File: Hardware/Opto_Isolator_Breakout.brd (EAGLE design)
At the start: 15.2 x 12.7 mm, 16 parts, among them Q1 NPN, Q2 NPN, U1 OPTO

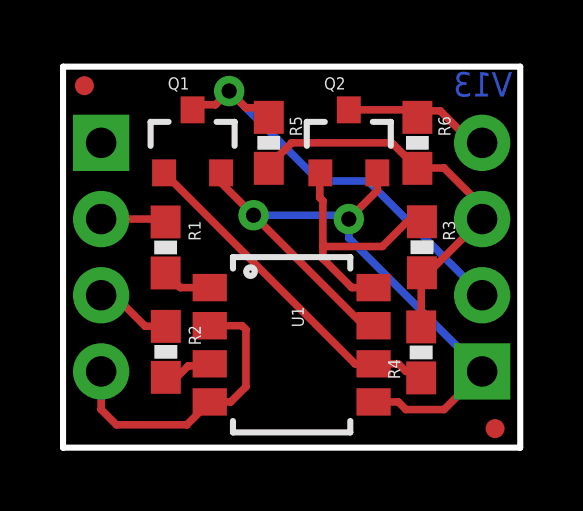
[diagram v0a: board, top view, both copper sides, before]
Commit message: Added attributes for IC IDL213T
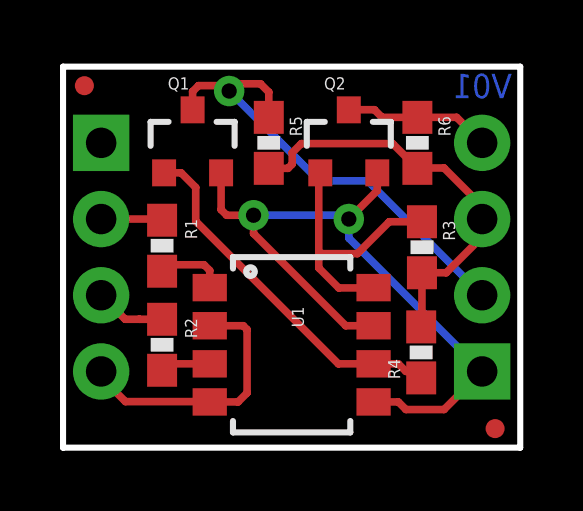
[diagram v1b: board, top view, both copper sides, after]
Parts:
- Q1, Q2: device SparkFun:SOT23-3 -> SparkFun-DiscreteSemi:SOT23-3
- R1, R2: value 200k -> 220
- U1: value OPTO -> OPTOISOLATOR-2SOIC8; device SparkFun:SO08-2 -> SparkFun-DiscreteSemi:SO08-2
- moved FRAME1 9.16 mm to (-22.7, -12.7)
- moved R2 0.27 mm to (3.30, 3.43)
- moved R1 0.13 mm to (3.30, 6.73)
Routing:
- net GND: track 10.00 -> 8.93 mm
- net OUT2: track 14.9 -> 15.9 mm
- net HV-GND: track 23.7 -> 24.6 mm
- net OUT2N: track 11.4 -> 12.1 mm
- net N$1: track 1.67 -> 2.33 mm
- net OUT1N: track 8.65 -> 9.25 mm
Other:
- board text added: "V01"
- board text removed: "V13"

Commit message: Fixed qc checklist issues.
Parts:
- FRAME1: value FRAME-LETTER -> (none)
- moved LOGO1 0.32 mm to (7.62, 8.45)
- moved LOGO2 0.16 mm to (8.71, 3.75)
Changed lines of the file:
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@@
 <setting verticaltext="up"/>
 </settings>
-<grid distance="0.05" unitdist="inch" unit="inch" style="lines" multiple="1" display="yes" altdistance="0.005" altunitdist="inch" altunit="inch"/>
+<grid distance="0.05" unitdist="inch" unit="inch" style="lines" multiple="1" display="yes" altdistance="0.00001" altunitdist="inch" altunit="inch"/>
 <layers>
 <layer number="1" name="Top" color="4" fill="1" visible="yes" active="yes"/>
@@
 <layer number="56" name="wert" color="7" fill="1" visible="no" active="yes"/>
 <layer number="57" name="tCAD" color="7" fill="1" visible="no" active="no"/>
+<layer number="59" name="tCarbon" color="7" fill="1" visible="no" active="no"/>
+<layer number="60" name="bCarbon" color="7" fill="1" visible="no" active="no"/>
 <layer number="90" name="Modules" color="5" fill="1" visible="no" active="no"/>
 <layer number="91" name="Nets" color="2" fill="1" visible="no" active="no"/>
@@
 <layer number="127" name="_tValues" color="7" fill="1" visible="no" active="yes"/>
 <layer number="128" name="_bValues" color="7" fill="1" visible="no" active="yes"/>
+<layer number="129" name="Mask" color="7" fill="1" visible="yes" active="yes"/>
 <layer number="131" name="tAdjust" color="7" fill="1" visible="no" active="yes"/>
 <layer number="132" name="bAdjust" color="7" fill="1" visible="no" active="yes"/>
@@
 <layer number="251" name="SMDround" color="12" fill="11" visible="no" active="no"/>
 <layer number="254" name="cooling" color="7" fill="1" visible="no" active="yes"/>
+<layer number="255" name="routoute" color="7" fill="1" visible="yes" active="yes"/>
 </layers>
 <board>
@@
 <element name="U$2" library="SparkFun-Aesthetics" package="MICRO-FIDUCIAL" value="FIDUCIALUFIDUCIAL" x="0.7112" y="12.065"/>
 <element name="U$3" library="SparkFun-Aesthetics" package="MICRO-FIDUCIAL" value="FIDUCIALUFIDUCIAL" x="14.4018" y="0.635"/>
-<element name="FRAME1" library="SparkFun-Aesthetics" package="CREATIVE_COMMONS" value="FRAME-LETTER" x="-22.7215875" y="-12.7"/>
-<element name="LOGO1" library="SparkFun-Aesthetics" package="OSHW-LOGO-S" value="OSHW-LOGOS" x="7.5946" y="8.128" rot="MR0"/>
-<element name="LOGO2" library="SparkFun-Aesthetics" package="SFE_LOGO_FLAME_.1" value="SFE_LOGO_FLAME.1_INCH" x="8.7503" y="3.596640625" rot="MR0"/>
+<element name="FRAME1" library="SparkFun-Aesthetics" package="CREATIVE_COMMONS" value="" x="-22.7215875" y="-12.7">
+<attribute name="VERSION" value="v01" x="-22.7215875" y="-12.7" size="1.778" layer="27" display="off"/>
+<attribute name="DESIGNER" value="NAME" x="-22.7215875" y="-12.7" size="1.778" layer="27" display="off"/>
+</element>
 <element name="R1" library="SparkFun-Resistors" package="0603-RES" value="220" x="3.302" y="6.731" rot="R270">
 <attribute name="PROD_ID" value="RES-07861" x="3.302" y="6.731" size="1.778" layer="27" font="vector" ratio="15" rot="R270" display="off"/>
@@
 <attribute name="PROD_ID" value="RES-07861" x="3.302" y="3.429" size="1.778" layer="27" font="vector" ratio="15" rot="R270" display="off"/>
 </element>
+<element name="LOGO2" library="SparkFun-Aesthetics" package="SFE_LOGO_FLAME_.1" value="SFE_LOGO_FLAME.1_INCH" x="8.710421875" y="3.750309375" rot="MR0"/>
+<element name="LOGO1" library="SparkFun-Aesthetics" package="OSHW-LOGO-S" value="OSHW-LOGOS" x="7.6233" y="8.45134375" rot="MR0"/>
 </elements>
 <signals>

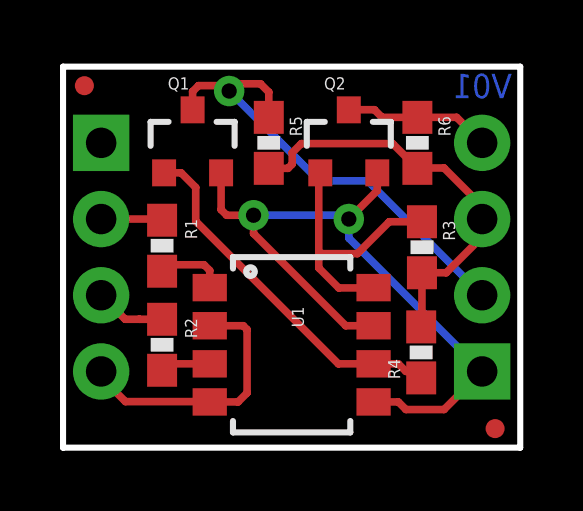
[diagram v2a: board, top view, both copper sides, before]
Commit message: Fixed final qc checklist items.
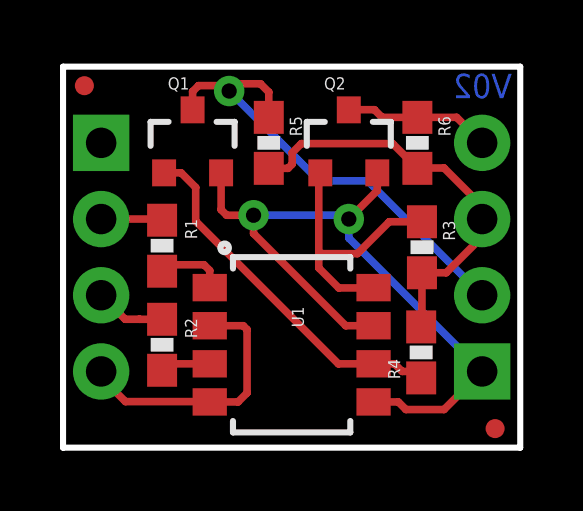
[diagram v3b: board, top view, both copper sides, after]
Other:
- board text added: "V02"
- board text removed: "V01"
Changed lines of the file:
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@@
 <?xml version="1.0" encoding="utf-8"?>
 <!DOCTYPE eagle SYSTEM "eagle.dtd">
-<eagle version="7.1.0">
+<eagle version="6.4">
 <drawing>
 <settings>
@@
 <setting verticaltext="up"/>
 </settings>
-<grid distance="0.05" unitdist="inch" unit="inch" style="lines" multiple="1" display="yes" altdistance="0.00001" altunitdist="inch" altunit="inch"/>
+<grid distance="0.05" unitdist="inch" unit="inch" style="lines" multiple="1" display="yes" altdistance="0.005" altunitdist="inch" altunit="inch"/>
 <layers>
 <layer number="1" name="Top" color="4" fill="1" visible="yes" active="yes"/>
@@
 <layer number="127" name="_tValues" color="7" fill="1" visible="no" active="yes"/>
 <layer number="128" name="_bValues" color="7" fill="1" visible="no" active="yes"/>
-<layer number="129" name="Mask" color="7" fill="1" visible="yes" active="yes"/>
+<layer number="129" name="Mask" color="7" fill="1" visible="no" active="yes"/>
 <layer number="131" name="tAdjust" color="7" fill="1" visible="no" active="yes"/>
 <layer number="132" name="bAdjust" color="7" fill="1" visible="no" active="yes"/>
@@
 <layer number="251" name="SMDround" color="12" fill="11" visible="no" active="no"/>
 <layer number="254" name="cooling" color="7" fill="1" visible="no" active="yes"/>
-<layer number="255" name="routoute" color="7" fill="1" visible="yes" active="yes"/>
+<layer number="255" name="routoute" color="7" fill="1" visible="no" active="yes"/>
 </layers>
 <board>
@@
 <text x="2.794" y="10.668" size="1.016" layer="22" font="vector" ratio="15" rot="MR180">NC</text>
 <text x="12.446" y="0.381" size="1.016" layer="22" font="vector" ratio="15" rot="MR0">Optoisolator</text>
-<text x="14.9606" y="11.6484375" size="0.8128" layer="16" font="vector" ratio="15" rot="MR0">V01</text>
+<text x="14.9606" y="11.6484375" size="0.8128" layer="16" font="vector" ratio="15" rot="MR0">V02</text>
 <text x="-11.140440625" y="-15.60068125" size="1.778" layer="51" font="vector" ratio="10">Revised by: Patrick Alberts</text>
 <text x="7.60221875" y="-12.867640625" size="1.778" layer="51" font="vector" ratio="10">N.Seidle</text>
@@
 <pass name="Default">
 <param name="RoutingGrid" value="50mil"/>
-<param name="AutoGrid" value="1"/>
-<param name="Efforts" value="0"/>
-<param name="TopRouterVariant" value="1"/>
 <param name="tpViaShape" value="round"/>
 <param name="PrefDir.1" value="|"/>
@@
 <contactref element="R4" pad="1"/>
 <contactref element="Q1" pad="1"/>
-<wire x1="10.3505" y1="2.794" x2="11.176" y2="2.794" width="0.254" layer="1"/>
-<wire x1="11.176" y1="2.794" x2="11.43" y2="2.54" width="0.254" layer="1"/>
-<wire x1="11.43" y1="2.54" x2="11.723" y2="2.54" width="0.254" layer="1"/>
+<wire x1="10.3505" y1="2.794" x2="11.049" y2="2.794" width="0.254" layer="1"/>
+<wire x1="11.049" y1="2.794" x2="11.303" y2="2.54" width="0.254" layer="1"/>
+<wire x1="11.303" y1="2.54" x2="11.723" y2="2.54" width="0.254" layer="1"/>
 <wire x1="11.723" y1="2.54" x2="11.938" y2="2.325" width="0.254" layer="1"/>
 <wire x1="3.368" y1="9.16" x2="3.936240625" y2="9.16" width="0.254" layer="1"/>

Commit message: Fixed QC checklist issues
Fixed version # in sch and brd
added "all units in inches" in layer 47
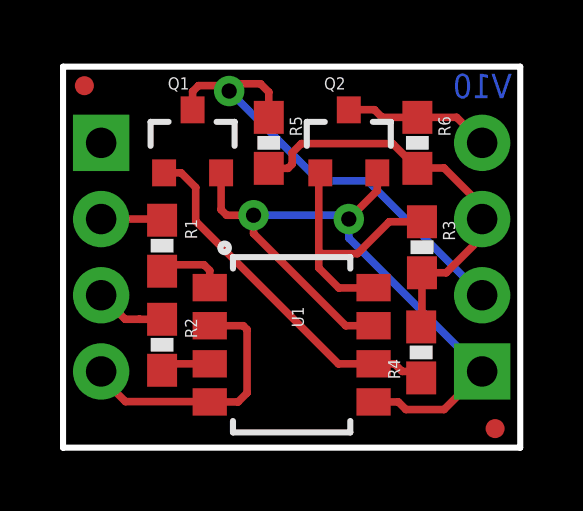
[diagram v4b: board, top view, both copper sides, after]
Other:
- board text added: "All units are in inches."
- board text added: "V10"
- board text removed: "V02"
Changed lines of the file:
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@@
 <?xml version="1.0" encoding="utf-8"?>
 <!DOCTYPE eagle SYSTEM "eagle.dtd">
-<eagle version="6.4">
+<eagle version="7.1.0">
 <drawing>
 <settings>
@@
 <layer number="45" name="Holes" color="7" fill="1" visible="yes" active="yes"/>
 <layer number="46" name="Milling" color="3" fill="1" visible="no" active="yes"/>
-<layer number="47" name="Measures" color="7" fill="1" visible="no" active="yes"/>
+<layer number="47" name="Measures" color="7" fill="1" visible="yes" active="yes"/>
 <layer number="48" name="Document" color="7" fill="1" visible="no" active="yes"/>
 <layer number="49" name="Reference" color="7" fill="1" visible="no" active="yes"/>
@@
 <text x="2.794" y="10.668" size="1.016" layer="22" font="vector" ratio="15" rot="MR180">NC</text>
 <text x="12.446" y="0.381" size="1.016" layer="22" font="vector" ratio="15" rot="MR0">Optoisolator</text>
-<text x="14.9606" y="11.6484375" size="0.8128" layer="16" font="vector" ratio="15" rot="MR0">V02</text>
+<text x="14.9606" y="11.6484375" size="0.8128" layer="16" font="vector" ratio="15" rot="MR0">V10</text>
 <text x="-11.140440625" y="-15.60068125" size="1.778" layer="51" font="vector" ratio="10">Revised by: Patrick Alberts</text>
 <text x="7.60221875" y="-12.867640625" size="1.778" layer="51" font="vector" ratio="10">N.Seidle</text>
 <dimension x1="-2.54" y1="12.7" x2="-2.54" y2="0" x3="-3.81" y3="6.35" textsize="1.778" textratio="15" layer="47" unit="inch"/>
 <dimension x1="0" y1="15.24" x2="15.24" y2="15.24" x3="7.62" y3="16.51" textsize="1.778" textratio="15" layer="47" unit="inch"/>
+<text x="-10.16" y="24.13" size="1.778" layer="47" font="vector" ratio="15">All units are in inches.</text>
 </plain>
 <attributes>
@@
 <pass name="Default">
 <param name="RoutingGrid" value="50mil"/>
+<param name="AutoGrid" value="1"/>
+<param name="Efforts" value="0"/>
+<param name="TopRouterVariant" value="1"/>
 <param name="tpViaShape" value="round"/>
 <param name="PrefDir.1" value="|"/>
